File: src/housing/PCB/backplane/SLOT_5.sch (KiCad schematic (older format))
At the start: 1 part, among them J2 10018784-10201TLF

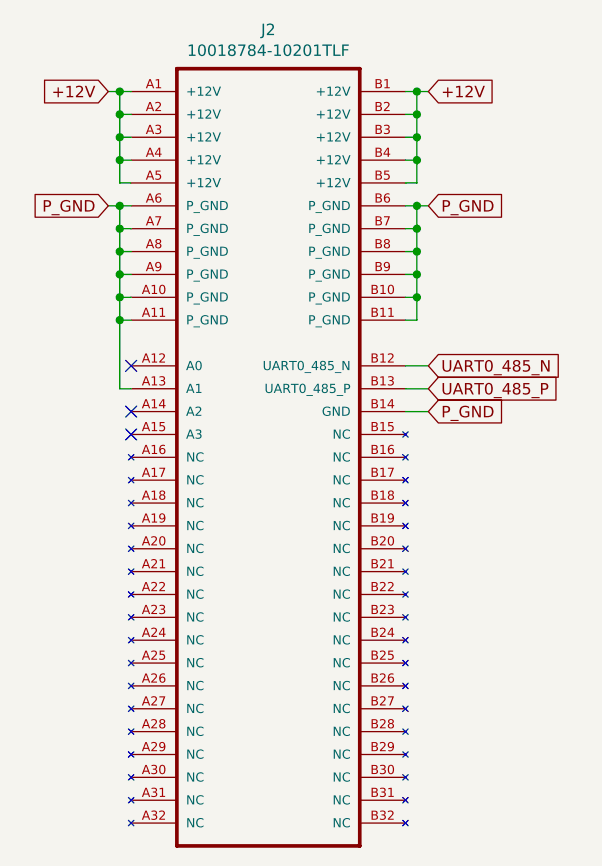
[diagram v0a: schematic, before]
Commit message: fixing backplane libraries path error
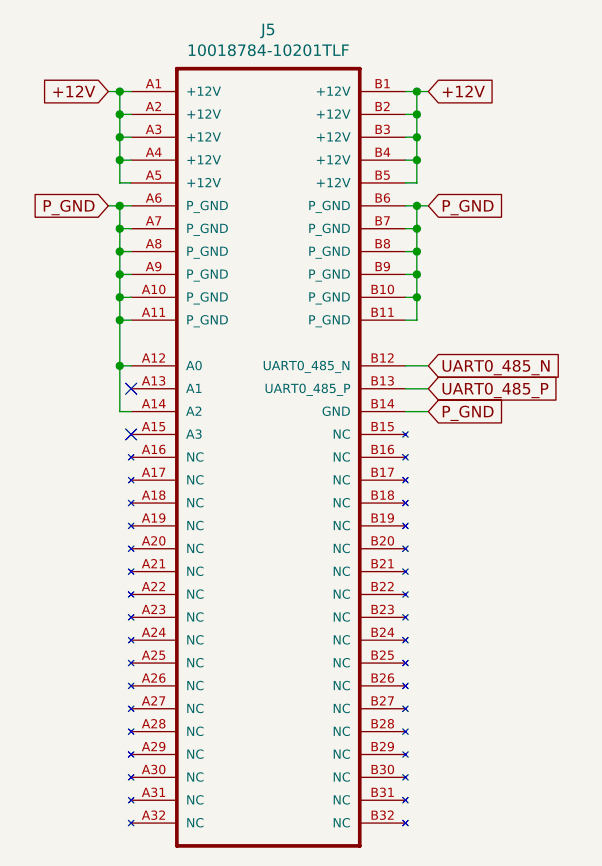
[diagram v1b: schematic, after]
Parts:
- removed J2: 10018784-10201TLF, kicad-lib:CONN_10018784-10201TLF, symbol 10018784-10201TLF:10018784-10201TLF
- added J5: 10018784-10201TLF, kicad-lib:CONN_10018784-10201TLF, symbol 10018784-10201TLF:10018784-10201TLF
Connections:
- net +12V: now also J5.A1 (+12V), J5.A2 (+12V), J5.A3 (+12V), J5.A4 (+12V), J5.A5 (+12V), J5.B1 (+12V), J5.B2 (+12V), J5.B3 (+12V), J5.B4 (+12V), J5.B5 (+12V)
- net P_GND: now also J5.A10 (P_GND), J5.A11 (P_GND), J5.A12 (A0), J5.A14 (A2), J5.A6 (P_GND), J5.A7 (P_GND), J5.A8 (P_GND), J5.A9 (P_GND), J5.B10 (P_GND), J5.B11 (P_GND), J5.B14 (GND), J5.B6 (P_GND), J5.B7 (P_GND), J5.B8 (P_GND), J5.B9 (P_GND)
- net UART0_485_N: now also J5.B12 (UART0_485_N)
- net UART0_485_P: now also J5.B13 (UART0_485_P)
- no-connect marks 3 -> 2
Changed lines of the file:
@@
 $Descr A4 11693 8268
 encoding utf-8
-Sheet 3 9
-Title ""
+Sheet 6 9
+Title "ACS backplane"
 Date ""
-Rev ""
-Comp ""
-Comment1 ""
+Rev "1"
+Comp "Halidelabs"
+Comment1 "contact@halidelabs.eu"
 Comment2 ""
 Comment3 ""
@@
 $Comp
 L 10018784-10201TLF:10018784-10201TLF J?
-U 1 1 5DF52F10
+U 1 1 5DF52F0D
 P 5600 3950
-AR Path="/5DF19C0C/5DF52F10" Ref="J?"  Part="1"
-AR Path="/5DF2A71E/5DF52F10" Ref="J?"  Part="1"
-AR Path="/5DF2E10A/5DF52F10" Ref="J2"  Part="1"
-AR Path="/5DF2E1F8/5DF52F10" Ref="J?"  Part="1"
-AR Path="/5DF2E248/5DF52F10" Ref="J?"  Part="1"
-AR Path="/5DF2E24C/5DF52F10" Ref="J?"  Part="1"
-F 0 "J2" H 5600 5820 50  0000 C CNN
+AR Path="/5DF19C0C/5DF52F0D" Ref="J?"  Part="1"
+AR Path="/5DF2A71E/5DF52F0D" Ref="J?"  Part="1"
+AR Path="/5DF2E10A/5DF52F0D" Ref="J?"  Part="1"
+AR Path="/5DF2E1F6/5DF52F0D" Ref="J?"  Part="1"
+AR Path="/5DF2E246/5DF52F0D" Ref="J5"  Part="1"
+AR Path="/5DF2E24A/5DF52F0D" Ref="J?"  Part="1"
+F 0 "J5" H 5600 5820 50  0000 C CNN
 F 1 "10018784-10201TLF" H 5600 5729 50  0000 C CNN
 F 2 "kicad-lib:CONN_10018784-10201TLF" H 5650 4450 50  0001 L BNN
@@
 Wire Wire Line
 	6300 3750 6200 3750
+Wire Wire Line
+	4950 3350 4950 3550
+Wire Wire Line
+	4950 3550 5000 3550
 Connection ~ 4950 3350
 Wire Wire Line
-	4950 3650 5000 3650
+	4950 3550 4950 3750
 Wire Wire Line
-	4950 3350 4950 3650
-NoConn ~ 5000 3550
-NoConn ~ 5000 3750
+	4950 3750 5000 3750
+Connection ~ 4950 3550
+NoConn ~ 5000 3650
 NoConn ~ 5000 3850
 $EndSCHEMATC
